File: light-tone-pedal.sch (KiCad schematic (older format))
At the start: 7 parts, among them U1 OPAMP

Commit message: Completed schematic of circuit in use for light-affected tone pedal.
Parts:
- removed Cpole1: 1u, symbol pspice:C
- removed RF1, Rpole1: 10k, symbol pspice:R
- removed U1: OPAMP, symbol pspice:OPAMP
- added C1: 0.1n, symbol pspice:CAP
- added C2, C3: 1u, symbol pspice:CAP
- added C_HIGH1: 5600p, symbol pspice:CAP
- added C_LOW1: 0.022u, symbol pspice:CAP
- added R1: 1k, symbol pspice:R
- added R2: 100k, symbol pspice:R
- added RG2, RG3, RG4: 1 Meg, symbol pspice:R
- added R_HIGH1, R_LOW1: 24k, symbol pspice:R
- added R_LDR1: 11k, symbol pspice:R
- added R_LDRLOW1: 3k, symbol pspice:R
- added R_POTVOL1, R_POTVOL2: 500k, symbol pspice:R
- added R_TONEPOT1, R_TONEPOT2: 5k, symbol pspice:R
- added U1: LM358AP, DIP254P762X508-8, symbol LM358AP:LM358AP
- RG1: value 1k -> 1 Meg
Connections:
- net labels added: OUT_BP, OUT_BUFFER, vout
- net labels removed: IN1+, IN1-, OUT1
- wire segments 25 -> 67
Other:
- moved on the sheet: VCC1, Vsignal1

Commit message: Fixed a mistake. Had wrong value for C1.
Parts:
- C1: value 0.1n -> 0.1u
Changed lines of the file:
@@
 P 4850 6300
 F 0 "C1" H 5028 6346 50  0000 L CNN
-F 1 "0.1n" H 5028 6255 50  0000 L CNN
+F 1 "0.1u" H 5028 6255 50  0000 L CNN
 F 2 "" H 4850 6300 50  0001 C CNN
 F 3 "~" H 4850 6300 50  0001 C CNN

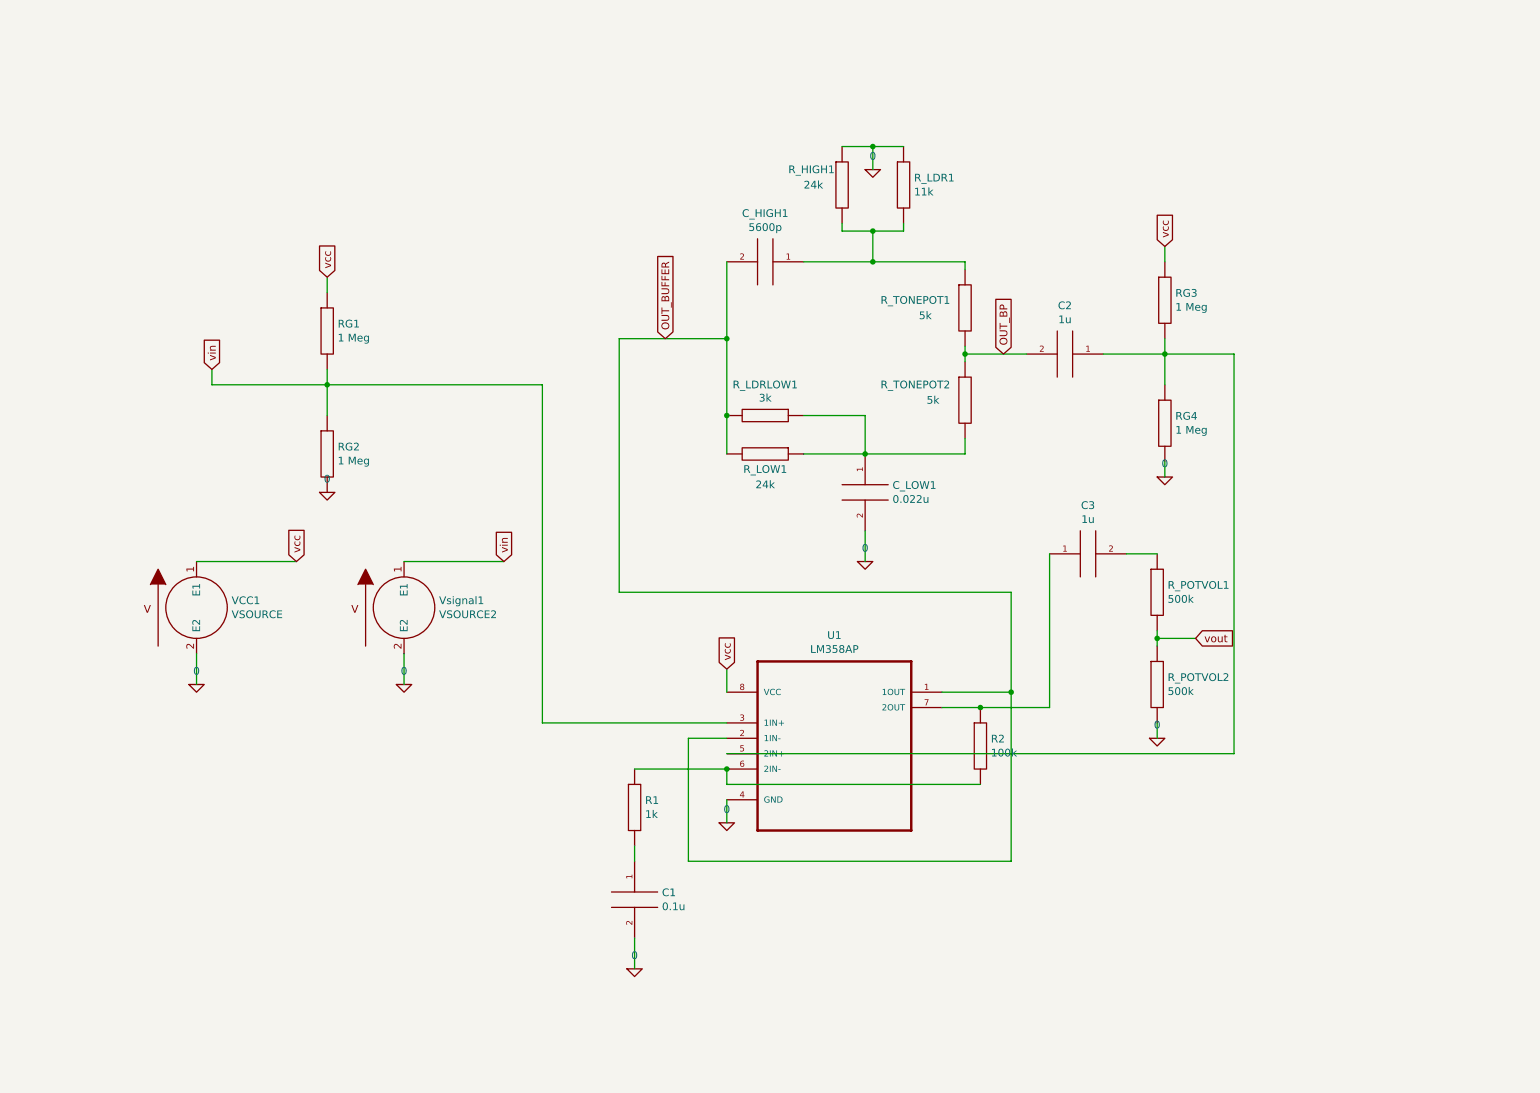
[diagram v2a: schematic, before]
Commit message: Added switch and signal generators. Also made pcb.
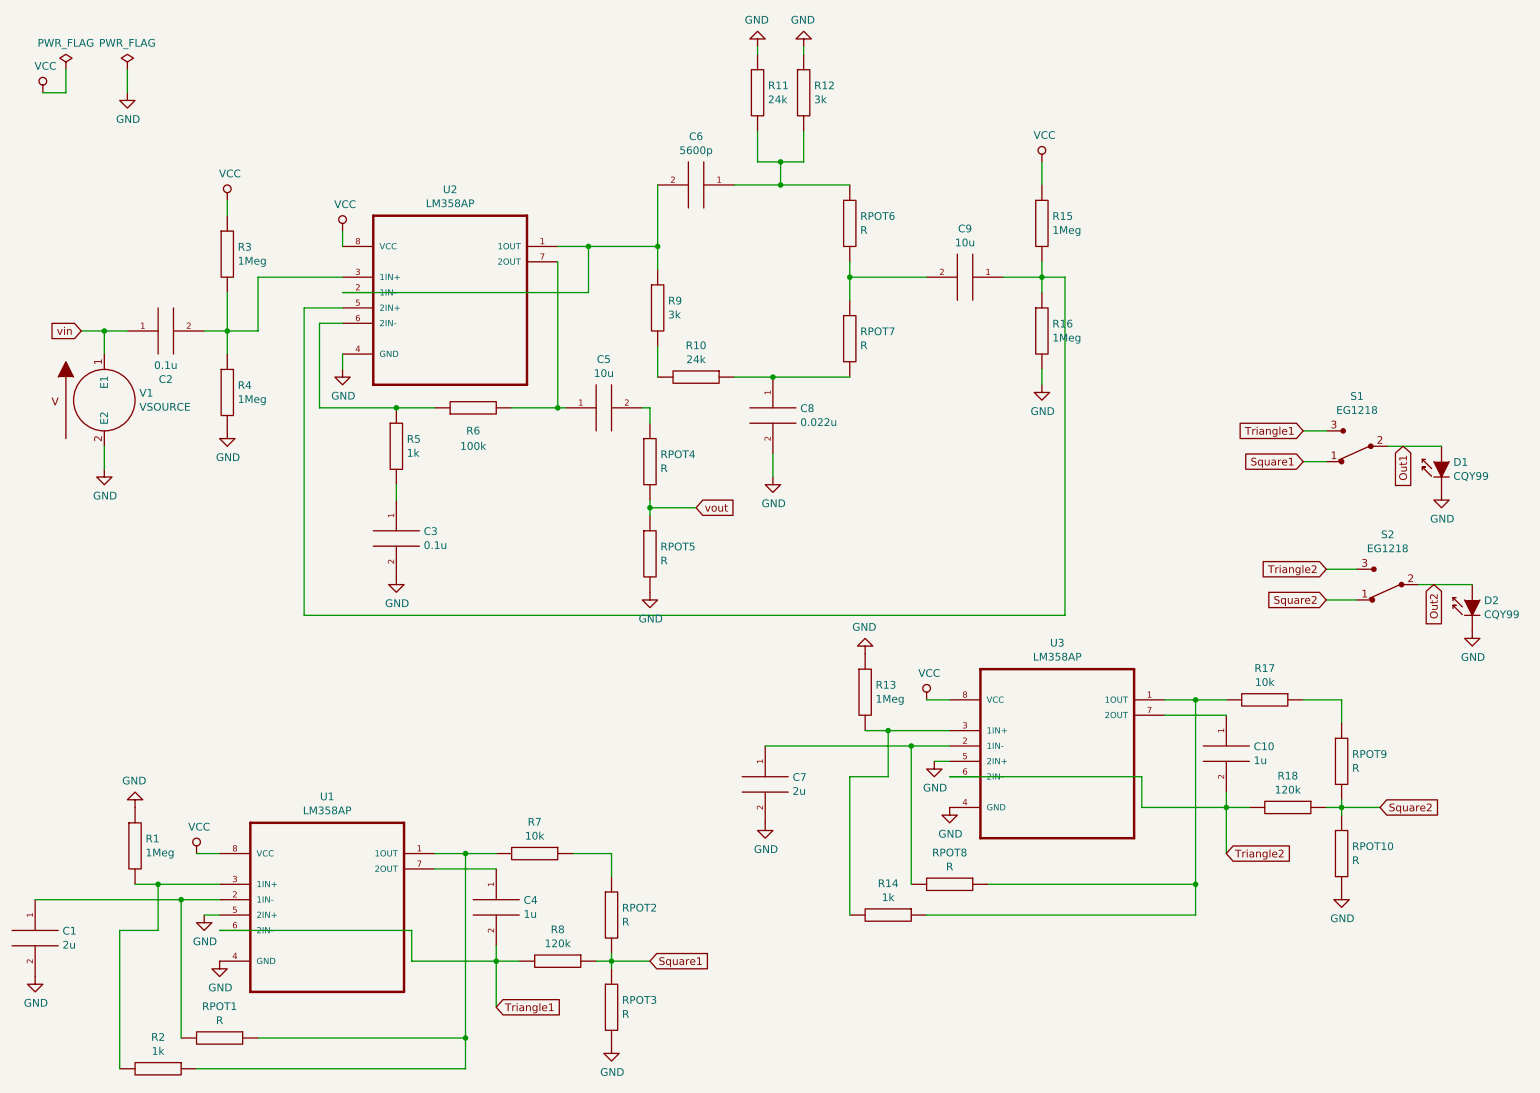
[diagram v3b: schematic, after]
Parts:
- removed C1: 0.1u, symbol pspice:CAP
- removed C2, C3: 1u, symbol pspice:CAP
- removed C_HIGH1: 5600p, symbol pspice:CAP
- removed C_LOW1: 0.022u, symbol pspice:CAP
- removed R1: 1k, symbol pspice:R
- removed R2: 100k, symbol pspice:R
- removed RG1, RG2, RG3, RG4: 1 Meg, symbol pspice:R
- removed R_HIGH1, R_LOW1: 24k, symbol pspice:R
- removed R_LDR1: 11k, symbol pspice:R
- removed R_LDRLOW1: 3k, symbol pspice:R
- removed R_POTVOL1, R_POTVOL2: 500k, symbol pspice:R
- removed R_TONEPOT1, R_TONEPOT2: 5k, symbol pspice:R
- removed VCC1: VSOURCE, symbol pspice:VSOURCE
- removed Vsignal1: VSOURCE2, symbol pspice:VSOURCE
- added C1, C7: 2u, Capacitor_THT:C_Rect_L29.0mm_W16.0mm_P27.50mm_MKT, symbol PSPICE:CAP
- added C10, C4: 1u, Capacitor_THT:C_Disc_D7.0mm_W2.5mm_P5.00mm, symbol PSPICE:CAP
- added C2, C3: 0.1u, Capacitor_THT:C_Disc_D7.0mm_W2.5mm_P5.00mm, symbol PSPICE:CAP
- added C5, C9: 10u, Capacitor_THT:C_Disc_D7.0mm_W2.5mm_P5.00mm, symbol PSPICE:CAP
- added C6: 5600p, Capacitor_THT:C_Rect_L24.0mm_W7.0mm_P22.50mm_MKT, symbol PSPICE:CAP
- added C8: 0.022u, Capacitor_THT:C_Rect_L13.0mm_W8.0mm_P10.00mm_FKS3_FKP3_MKS4, symbol PSPICE:CAP
- added D1, D2: CQY99, LED_THT:LED_D3.0mm, symbol Diode:CQY99
- added R1, R13, R15, R16, R3, R4: 1Meg, Resistor_THT:R_Axial_DIN0207_L6.3mm_D2.5mm_P7.62mm_Horizontal, symbol PSPICE:R
- added R10, R11: 24k, Resistor_THT:R_Axial_DIN0207_L6.3mm_D2.5mm_P7.62mm_Horizontal, symbol PSPICE:R
- added R12, R9: 3k, Resistor_THT:R_Axial_DIN0207_L6.3mm_D2.5mm_P7.62mm_Horizontal, symbol PSPICE:R
- added R14, R2, R5: 1k, Resistor_THT:R_Axial_DIN0207_L6.3mm_D2.5mm_P7.62mm_Horizontal, symbol PSPICE:R
- added R17, R7: 10k, Resistor_THT:R_Axial_DIN0207_L6.3mm_D2.5mm_P7.62mm_Horizontal, symbol PSPICE:R
- added R18, R8: 120k, Resistor_THT:R_Axial_DIN0207_L6.3mm_D2.5mm_P7.62mm_Horizontal, symbol PSPICE:R
- added R6: 100k, Resistor_THT:R_Axial_DIN0207_L6.3mm_D2.5mm_P7.62mm_Horizontal, symbol PSPICE:R
- added RPOT1, RPOT10, RPOT2, RPOT3, RPOT4, RPOT5, RPOT6, RPOT7, RPOT8, RPOT9: R, Resistor_THT:R_Axial_DIN0207_L6.3mm_D2.5mm_P7.62mm_Horizontal, symbol PSPICE:R
- added S1, S2: EG1218, light-affected-tone-pedal:Switch_Slide_11.6x4mm_EG1218, symbol light-affected-tone-pedal:EG1218
- added U2, U3: LM358AP, light-affected-tone-pedal:DIP254P762X508-8, symbol LM358AP:LM358AP
- added V1: VSOURCE, Resistor_THT:R_Axial_DIN0207_L6.3mm_D2.5mm_P7.62mm_Horizontal, symbol PSPICE:VSOURCE
- U1: footprint DIP254P762X508-8 -> light-affected-tone-pedal:DIP254P762X508-8; Field4 LM358AP -> 296-9554-5-ND; Field5 DIP-8 Texas Instruments -> Dual Operational Amplifier 8-PDIP 0 to 70; Field6 Texas Instruments -> https://www.digikey.com/product-detail/en/texas-instruments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; Field7 https://www.digikey.com/product-detail/en/texas-instruments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 -> LM358AP; Field8 296-9554-5-ND -> DIP-8 Texas Instruments
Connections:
- net 0 is gone; now on net GND: U1.4 (GND)
- net vin: now also C2.1, V1.1 (E1); no longer U1.3 (1IN+)
- net vout: now also RPOT4.2, RPOT5.1
- net GND: now reaches U1.5 (2IN+)
- net GND: now also C1.2, C3.2, C7.2, C8.2, D1.1 (K), D2.1 (K), R1.1, R11.1, R12.1, R13.1, R16.2, R4.2, RPOT10.2, RPOT3.2, RPOT5.2, U2.4 (GND), U3.4 (GND), U3.5 (2IN+), V1.2 (E2)
- net Triangle1: now reaches U1.6 (2IN-)
- net Triangle1: now also C4.2, R8.2, S1.3
- net at U1.7 (2OUT): now also C4.1
- net OUT_BUFFER: no longer names the net of U1.1 (1OUT)
- net OUT_BUFFER: now also R2.1, R7.2, RPOT1.1; no longer U1.2 (1IN-)
- net vcc renamed VCC
- net VCC: now also R15.1, R3.1, U2.8 (VCC), U3.8 (VCC)
- new net: C6.2, R9.1, U2.1 (1OUT), U2.2 (1IN-)
- new net: C2.2, R3.2, R4.1, U2.3 (1IN+)
- new net: C9.1, R15.2, R16.1, U2.5 (2IN+)
- new net: R5.1, R6.1, U2.6 (2IN-)
- new net: C5.1, R6.2, U2.7 (2OUT)
- new net: C1.1, RPOT1.2, U1.2 (1IN-)
- new net: R1.2, R2.2, U1.3 (1IN+)
- new net: C9.2, RPOT6.2, RPOT7.1
- new net: R10.2, R9.2
- new net: C8.1, R10.1, RPOT7.2
- new net: C6.1, R11.2, R12.2, RPOT6.1
- new net: R7.1, RPOT2.1
- new net: C3.1, R5.2
- new net: C5.2, RPOT4.1
- new net: R14.1, R17.2, RPOT8.1, U3.1 (1OUT)
- new net: C7.1, RPOT8.2, U3.2 (1IN-)
- new net: R13.2, R14.2, U3.3 (1IN+)
- new net: C10.1, U3.7 (2OUT)
- new net: R17.1, RPOT9.1
- new net Out1: D1.2 (A), S1.2
- new net Out2: D2.2 (A), S2.2
- new net Square1: R8.1, RPOT2.2, RPOT3.1, S1.1
- new net Square2: R18.1, RPOT10.1, RPOT9.2, S2.1
- new net Triangle2: C10.2, R18.2, S2.3, U3.6 (2IN-)

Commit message: Updated pdf of circuit schematic. Made pcb for light affected tone pedal.
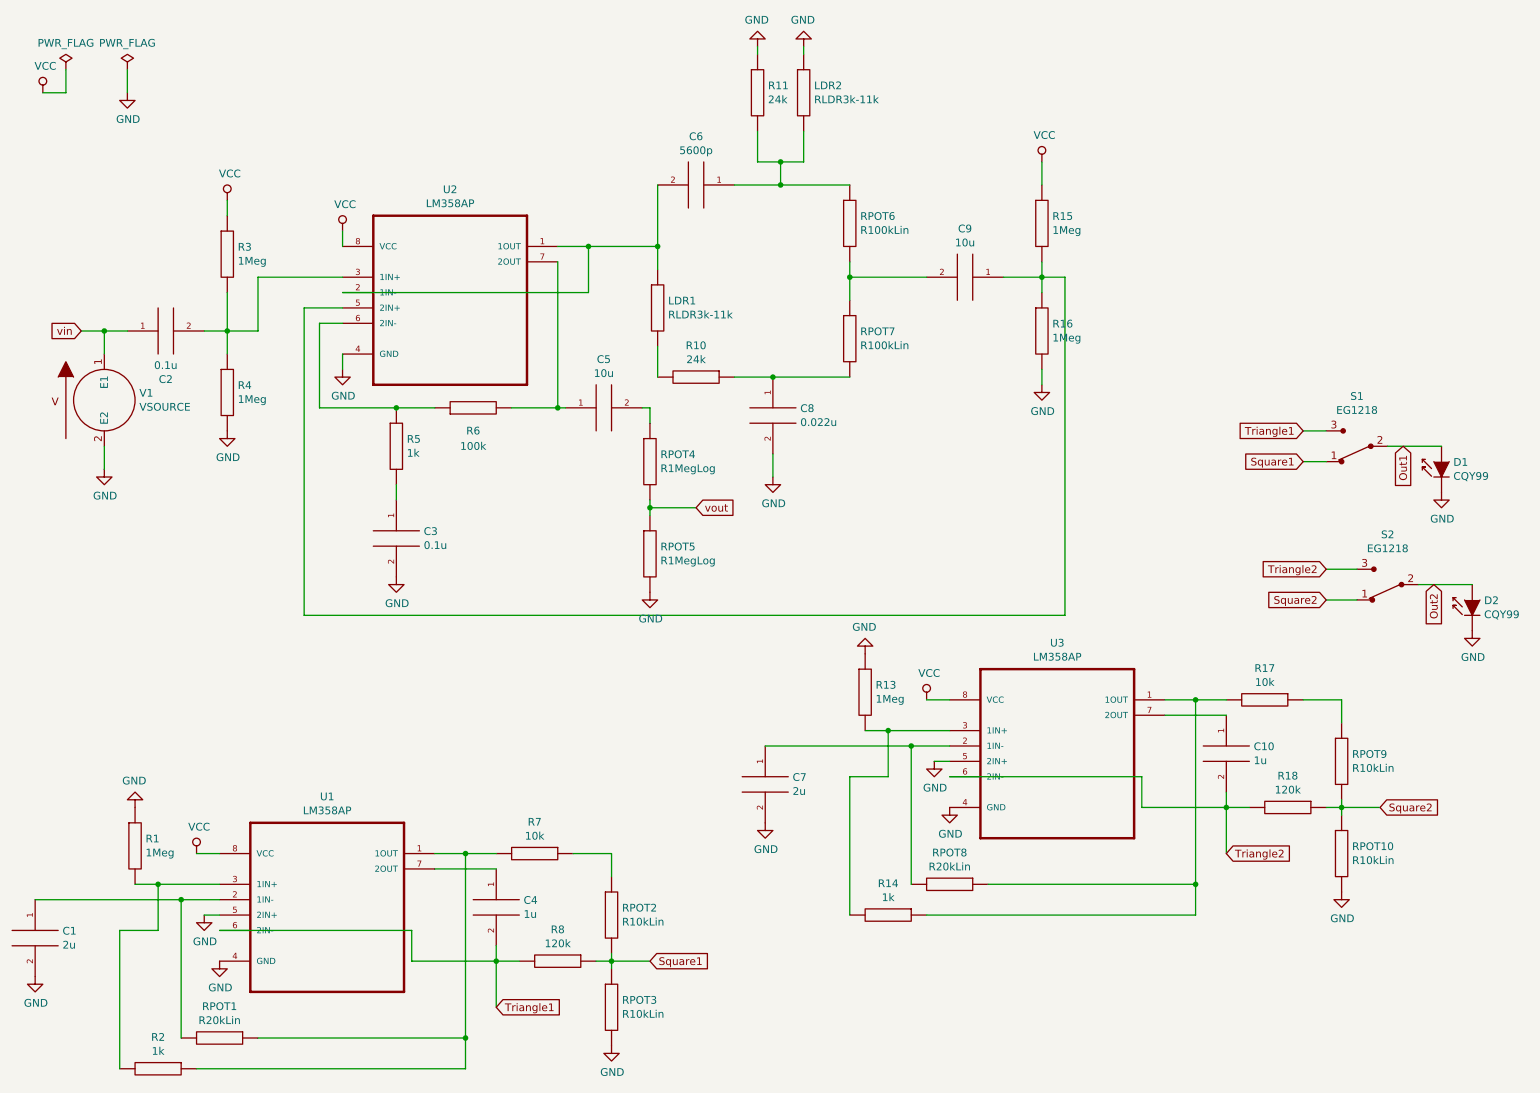
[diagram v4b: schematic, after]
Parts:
- LDR1: renamed from R9; value 3k -> RLDR3k-11k
- LDR2: renamed from R12; value 3k -> RLDR3k-11k
- RPOT1, RPOT8: value R -> R20kLin
- RPOT10, RPOT2, RPOT3, RPOT9: value R -> R10kLin
- RPOT4, RPOT5: value R -> R1MegLog
- RPOT6, RPOT7: value R -> R100kLin
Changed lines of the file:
@@
 	7500 2850 7500 2950
 $Comp
-L PSPICE:R R9
+L PSPICE:R LDR1
 U 1 1 5CFA2BB6
 P 5000 2450
-F 0 "R9" H 5068 2496 50  0000 L CNN
-F 1 "3k" H 5068 2405 50  0000 L CNN
+F 0 "LDR1" H 5068 2496 50  0000 L CNN
+F 1 "RLDR3k-11k" H 5068 2405 50  0000 L CNN
 F 2 "Resistor_THT:R_Axial_DIN0207_L6.3mm_D2.5mm_P7.62mm_Horizontal" H 5000 2450 50  0001 C CNN
 F 3 "~" H 5000 2450 50  0001 C CNN
@@
 $EndComp
 $Comp
-L PSPICE:R R12
+L PSPICE:R LDR2
 U 1 1 5CFA51BB
 P 5950 1050
-F 0 "R12" H 6018 1096 50  0000 L CNN
-F 1 "3k" H 6018 1005 50  0000 L CNN
+F 0 "LDR2" H 6018 1096 50  0000 L CNN
+F 1 "RLDR3k-11k" H 6018 1005 50  0000 L CNN
 F 2 "Resistor_THT:R_Axial_DIN0207_L6.3mm_D2.5mm_P7.62mm_Horizontal" H 5950 1050 50  0001 C CNN
 F 3 "~" H 5950 1050 50  0001 C CNN
@@
 P 6250 1900
 F 0 "RPOT6" H 6318 1946 50  0000 L CNN
-F 1 "R" H 6318 1855 50  0000 L CNN
+F 1 "R100kLin" H 6318 1855 50  0000 L CNN
 F 2 "Resistor_THT:R_Axial_DIN0207_L6.3mm_D2.5mm_P7.62mm_Horizontal" H 6250 1900 50  0001 C CNN
 F 3 "~" H 6250 1900 50  0001 C CNN
@@
 P 6250 2650
 F 0 "RPOT7" H 6318 2696 50  0000 L CNN
-F 1 "R" H 6318 2605 50  0000 L CNN
+F 1 "R100kLin" H 6318 2605 50  0000 L CNN
 F 2 "Resistor_THT:R_Axial_DIN0207_L6.3mm_D2.5mm_P7.62mm_Horizontal" H 6250 2650 50  0001 C CNN
 F 3 "~" H 6250 2650 50  0001 C CNN
@@
 P 4950 3450
 F 0 "RPOT4" H 5018 3496 50  0000 L CNN
-F 1 "R" H 5018 3405 50  0000 L CNN
+F 1 "R1MegLog" H 5018 3405 50  0000 L CNN
 F 2 "Resistor_THT:R_Axial_DIN0207_L6.3mm_D2.5mm_P7.62mm_Horizontal" H 4950 3450 50  0001 C CNN
 F 3 "~" H 4950 3450 50  0001 C CNN
@@
 P 4950 4050
 F 0 "RPOT5" H 5018 4096 50  0000 L CNN
-F 1 "R" H 5018 4005 50  0000 L CNN
+F 1 "R1MegLog" H 5018 4005 50  0000 L CNN
 F 2 "Resistor_THT:R_Axial_DIN0207_L6.3mm_D2.5mm_P7.62mm_Horizontal" H 4950 4050 50  0001 C CNN
 F 3 "~" H 4950 4050 50  0001 C CNN
@@
 P 2150 7200
 F 0 "RPOT1" V 1945 7200 50  0000 C CNN
-F 1 "R" V 2036 7200 50  0000 C CNN
+F 1 "R20kLin" V 2036 7200 50  0000 C CNN
 F 2 "Resistor_THT:R_Axial_DIN0207_L6.3mm_D2.5mm_P7.62mm_Horizontal" H 2150 7200 50  0001 C CNN
 F 3 "~" H 2150 7200 50  0001 C CNN
@@
 P 4700 6400
 F 0 "RPOT2" H 4768 6446 50  0000 L CNN
-F 1 "R" H 4768 6355 50  0000 L CNN
+F 1 "R10kLin" H 4768 6355 50  0000 L CNN
 F 2 "Resistor_THT:R_Axial_DIN0207_L6.3mm_D2.5mm_P7.62mm_Horizontal" H 4700 6400 50  0001 C CNN
 F 3 "~" H 4700 6400 50  0001 C CNN
@@
 P 4700 7000
 F 0 "RPOT3" H 4768 7046 50  0000 L CNN
-F 1 "R" H 4768 6955 50  0000 L CNN
+F 1 "R10kLin" H 4768 6955 50  0000 L CNN
 F 2 "Resistor_THT:R_Axial_DIN0207_L6.3mm_D2.5mm_P7.62mm_Horizontal" H 4700 7000 50  0001 C CNN
 F 3 "~" H 4700 7000 50  0001 C CNN
@@
 P 6900 6200
 F 0 "RPOT8" V 6695 6200 50  0000 C CNN
-F 1 "R" V 6786 6200 50  0000 C CNN
+F 1 "R20kLin" V 6786 6200 50  0000 C CNN
 F 2 "Resistor_THT:R_Axial_DIN0207_L6.3mm_D2.5mm_P7.62mm_Horizontal" H 6900 6200 50  0001 C CNN
 F 3 "~" H 6900 6200 50  0001 C CNN
@@
 P 9450 5400
 F 0 "RPOT9" H 9518 5446 50  0000 L CNN
-F 1 "R" H 9518 5355 50  0000 L CNN
+F 1 "R10kLin" H 9518 5355 50  0000 L CNN
 F 2 "Resistor_THT:R_Axial_DIN0207_L6.3mm_D2.5mm_P7.62mm_Horizontal" H 9450 5400 50  0001 C CNN
 F 3 "~" H 9450 5400 50  0001 C CNN
@@
 P 9450 6000
 F 0 "RPOT10" H 9518 6046 50  0000 L CNN
-F 1 "R" H 9518 5955 50  0000 L CNN
+F 1 "R10kLin" H 9518 5955 50  0000 L CNN
 F 2 "Resistor_THT:R_Axial_DIN0207_L6.3mm_D2.5mm_P7.62mm_Horizontal" H 9450 6000 50  0001 C CNN
 F 3 "~" H 9450 6000 50  0001 C CNN
